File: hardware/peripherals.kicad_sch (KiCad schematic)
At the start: 0 parts

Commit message: First draft of audio amplifier
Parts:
- added C1: 0.1µF, symbol Device:C
- added C2: 10µF, symbol Device:C
- added C3, C4: 220pF, symbol Device:C
- added FB1, FB2: FerriteBead_Small, symbol Device:FerriteBead_Small
- added R1: 1M, symbol Device:R
- added U1: MAX98357A, Package_DFN_QFN:TQFN-16-1EP_3x3mm_P0.5mm_EP1.23x1.23mm, symbol Audio:MAX98357A
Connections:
- new net: C4.1, FB1.2
- new net: C1.1, C2.1, U1.7 (VDD), U1.8 (VDD)
- new net: R1.2, U1.1 (DIN)
- new net: FB2.1, U1.10 (OUTN)
- new net: FB1.1, U1.9 (OUTP)
- new net: C3.1, FB2.2
- new net GND: C1.2, C2.2, C3.2, C4.2, U1.11 (GND), U1.15 (GND), U1.3 (GND)
- no-connect marks 0 -> 1

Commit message: Updating audio amplifier
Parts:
- added J1: Conn_01x02, symbol Connector_Generic:Conn_01x02
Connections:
- net SPEAKER_VO+: now reaches C4.1, FB1.2
- net SPEAKER_VO+: now also J1.1 (Pin_1)
- net +5V: now reaches C1.1, C2.1, U1.7 (VDD), U1.8 (VDD)
- net +5V: now also R1.1
- net SPEAKER_VO-: now reaches C3.1, FB2.2
- net SPEAKER_VO-: now also J1.2 (Pin_2)

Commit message: Adding IMU
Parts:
- added U2: BNO055, Package_LGA:LGA-28_5.2x3.8mm_P0.5mm, symbol Sensor_Motion:BNO055
- renumbered C4 to C?, C2 to C?, C3 to C?, C1 to C?, FB1 to FB?, FB2 to FB?, J1 to J?, R1 to R?, U1 to U?
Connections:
- net GND: now also U?.17 (PAD)
- net at R?.2: now also U?.4 (~{SD_MODE}); no longer U?.1 (DIN)
- net LRCLK: now reaches U?.14 (LRCLK)
- net BCLK: now reaches U?.16 (BCLK)
- net GAIN: now reaches U?.2 (GAIN_SLOT)
- new net DIN: U?.1 (DIN)
- no-connect marks 1 -> 0
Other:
- moved on the sheet: R?

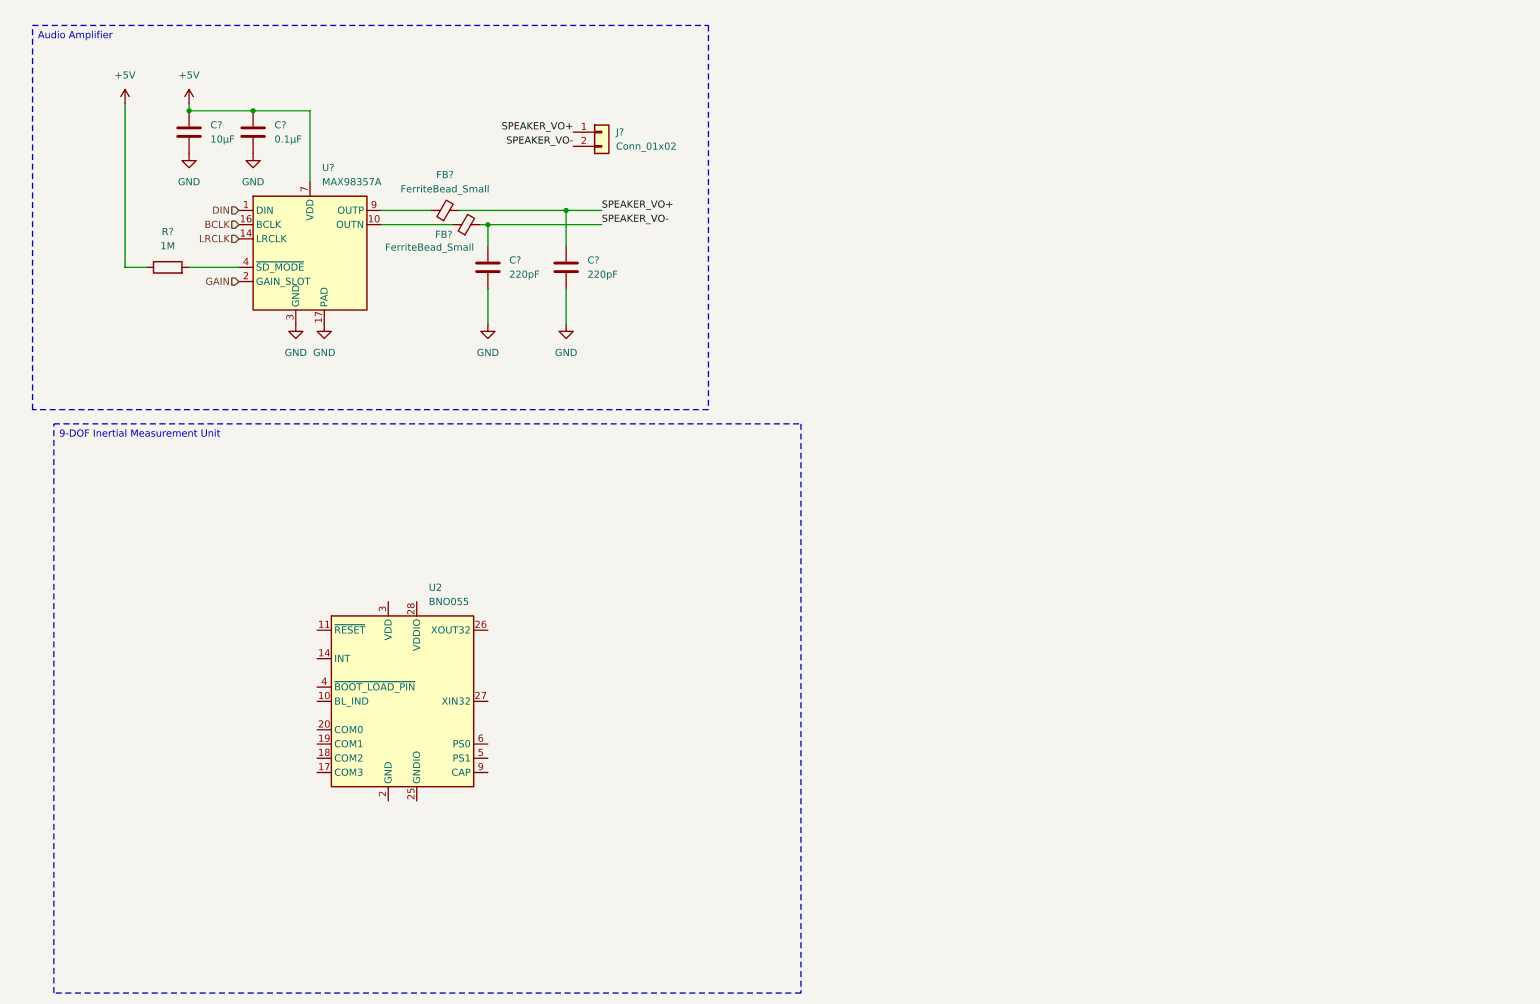
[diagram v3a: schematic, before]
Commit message: Finishing IMU schematic
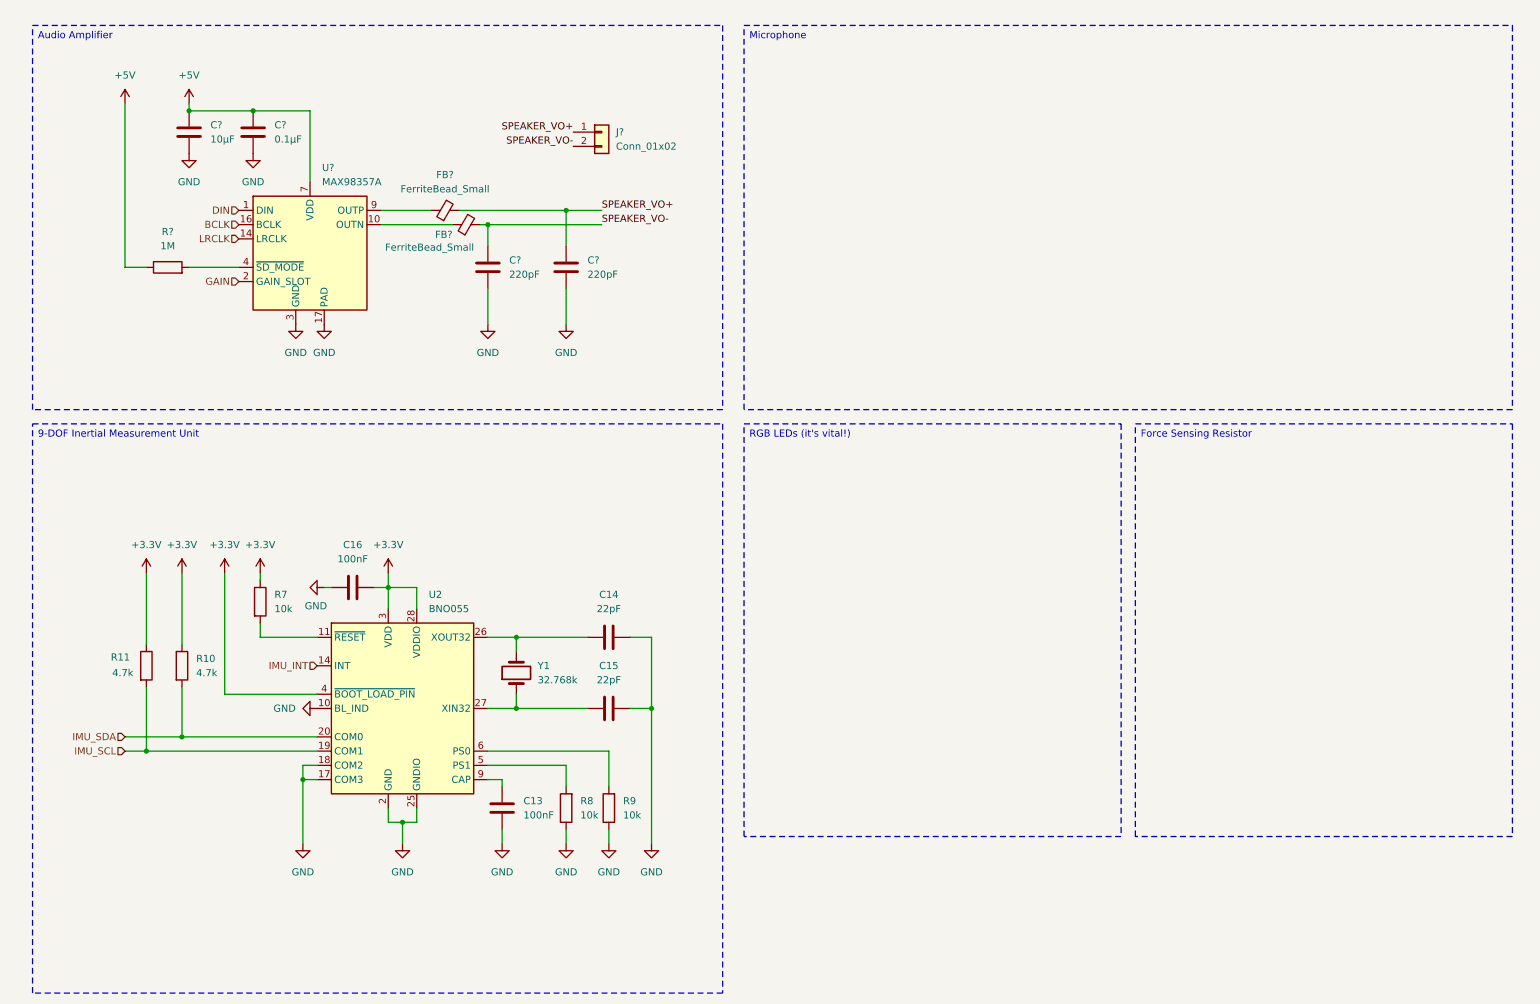
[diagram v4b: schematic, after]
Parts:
- added C13, C16: 100nF, symbol Device:C
- added C14, C15: 22pF, symbol Device:C
- added R10, R11: 4.7k, symbol Device:R
- added R7, R8, R9: 10k, symbol Device:R
- added Y1: 32.768k, symbol Device:Crystal
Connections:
- net GND: now also U2.10 (BL_IND), U2.17 (COM3), U2.18 (COM2), U2.2 (GND), U2.25 (GNDIO), C13.2, C14.2, C15.2, C16.1, R8.1, R9.1
- net at U2.11 (~{RESET}): now also R7.2
- net IMU_INT: now reaches U2.14 (INT)
- net IMU_SCL: now reaches U2.19 (COM1)
- net IMU_SCL: now also R11.2
- net IMU_SDA: now reaches U2.20 (COM0)
- net IMU_SDA: now also R10.2
- net at U2.26 (XOUT32): now also C14.1, Y1.2
- net at U2.27 (XIN32): now also C15.1, Y1.1
- net +3.3V: now reaches U2.28 (VDDIO)
- net +3.3V: now also U2.3 (VDD), U2.4 (~{BOOT_LOAD_PIN}), C16.2, R10.1, R11.1, R7.1
- net at U2.5 (PS1): now also R8.2
- net at U2.6 (PS0): now also R9.2
- net at U2.9 (CAP): now also C13.1
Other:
- moved on the sheet: U2

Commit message: Adding Force Resistive Sensor
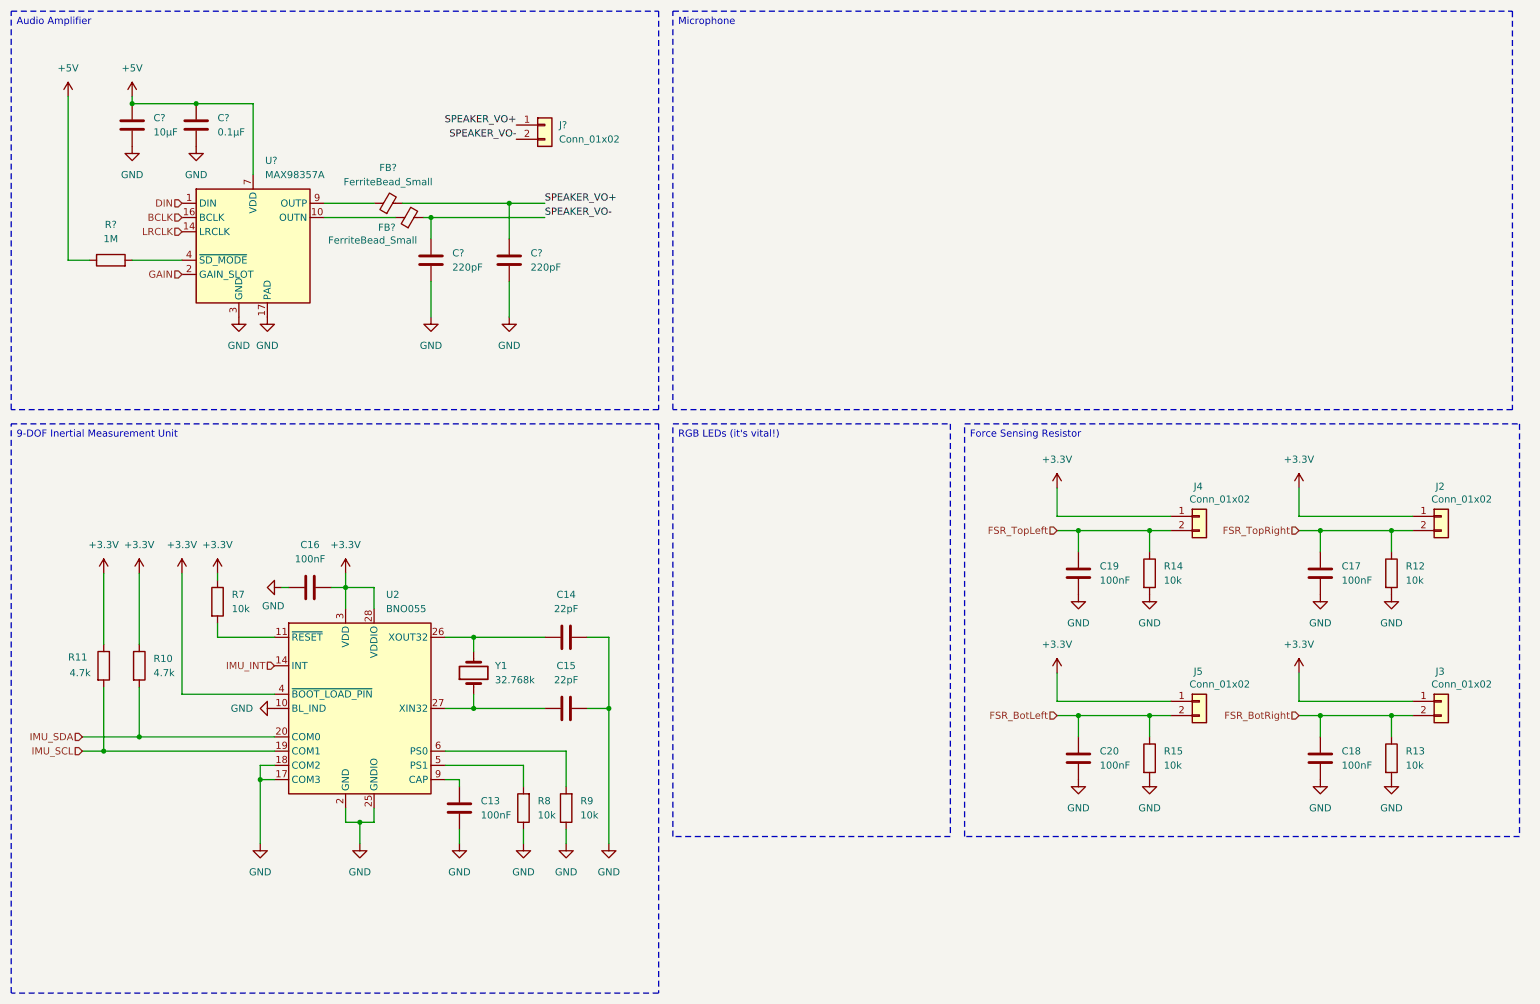
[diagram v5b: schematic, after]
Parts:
- added C17, C18, C19, C20: 100nF, symbol Device:C
- added J2, J3, J4, J5: Conn_01x02, symbol Connector_Generic:Conn_01x02
- added R12, R13, R14, R15: 10k, symbol Device:R
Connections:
- net +3.3V: now also J2.1 (Pin_1), J3.1 (Pin_1), J4.1 (Pin_1), J5.1 (Pin_1)
- net GND: now also C17.2, C18.2, C19.2, C20.2, R12.2, R13.2, R14.2, R15.2
- new net FSR_BotLeft: C20.1, J5.2 (Pin_2), R15.1
- new net FSR_BotRight: C18.1, J3.2 (Pin_2), R13.1
- new net FSR_TopLeft: C19.1, J4.2 (Pin_2), R14.1
- new net FSR_TopRight: C17.1, J2.2 (Pin_2), R12.1
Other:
- moved on the sheet: C13, C14, C15, C16, C?, FB?, J?, R10, R11, R7, R8, R9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

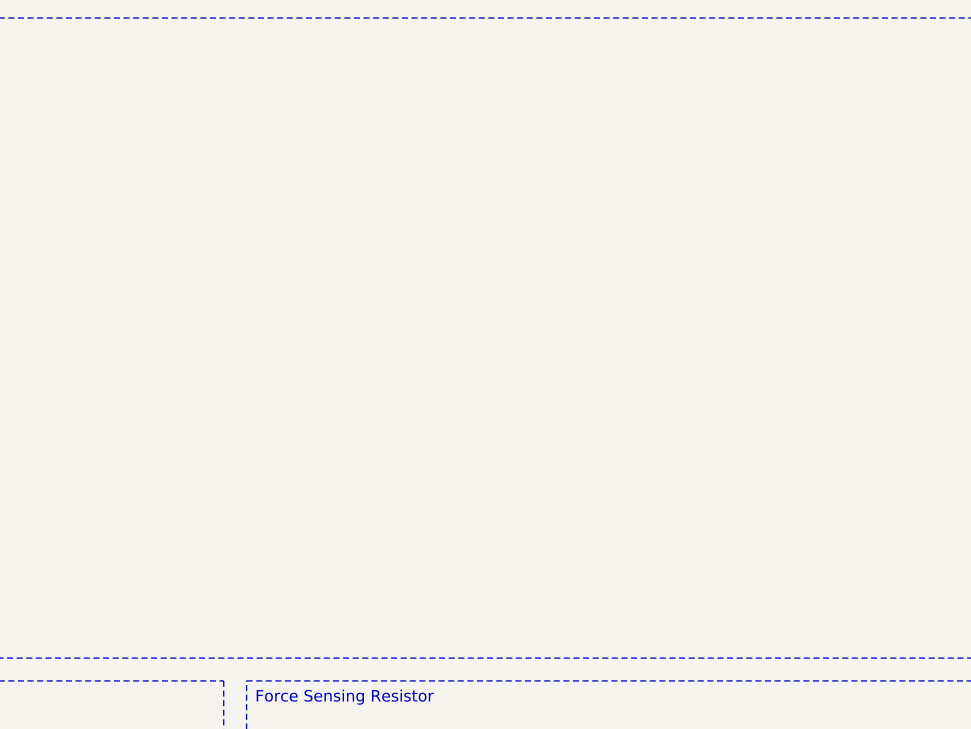
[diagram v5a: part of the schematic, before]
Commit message: Updating microphone schematic
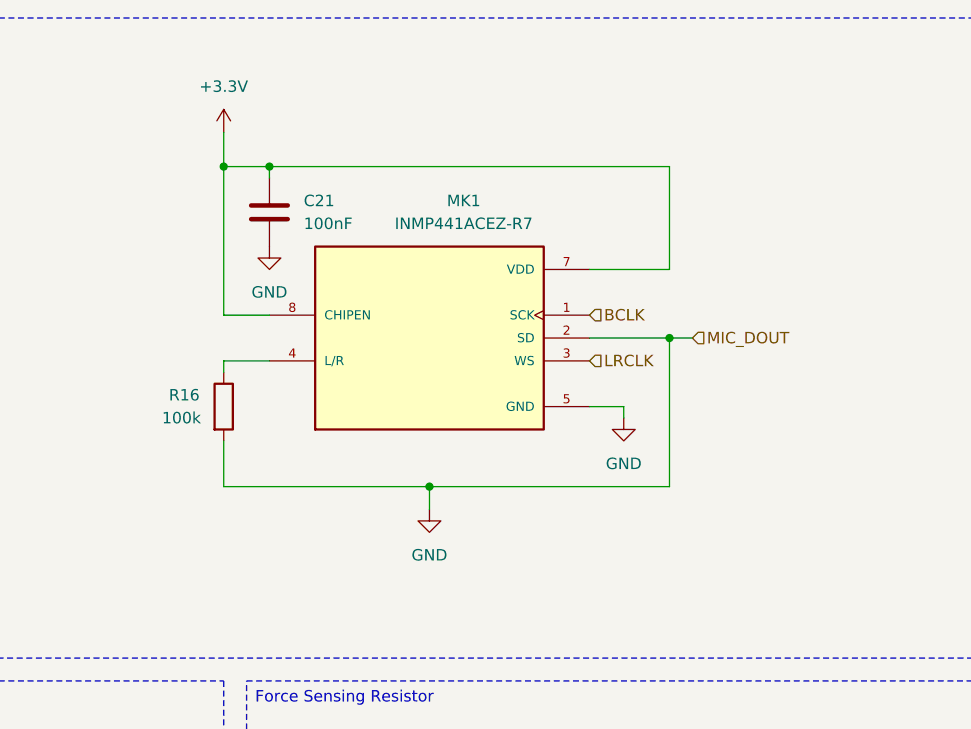
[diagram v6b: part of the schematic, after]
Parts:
- added C21: 100nF, symbol Device:C
- added MK1: INMP441ACEZ-R7, INMP441ACEZ-R7:MIC_INMP441ACEZ-R7, symbol INMP441ACEZ-R7:INMP441ACEZ-R7
- added R16: 100k, symbol Device:R
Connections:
- net +3.3V: now also C21.1, MK1.7 (VDD), MK1.8 (CHIPEN)
- net BCLK: now also MK1.1 (SCK)
- net GND: now also C21.2, MK1.2 (SD), MK1.5 (GND), MK1.6 (GND), MK1.9 (GND), R16.2
- net LRCLK: now also MK1.3 (WS)
- new net: MK1.4 (L/R), R16.1

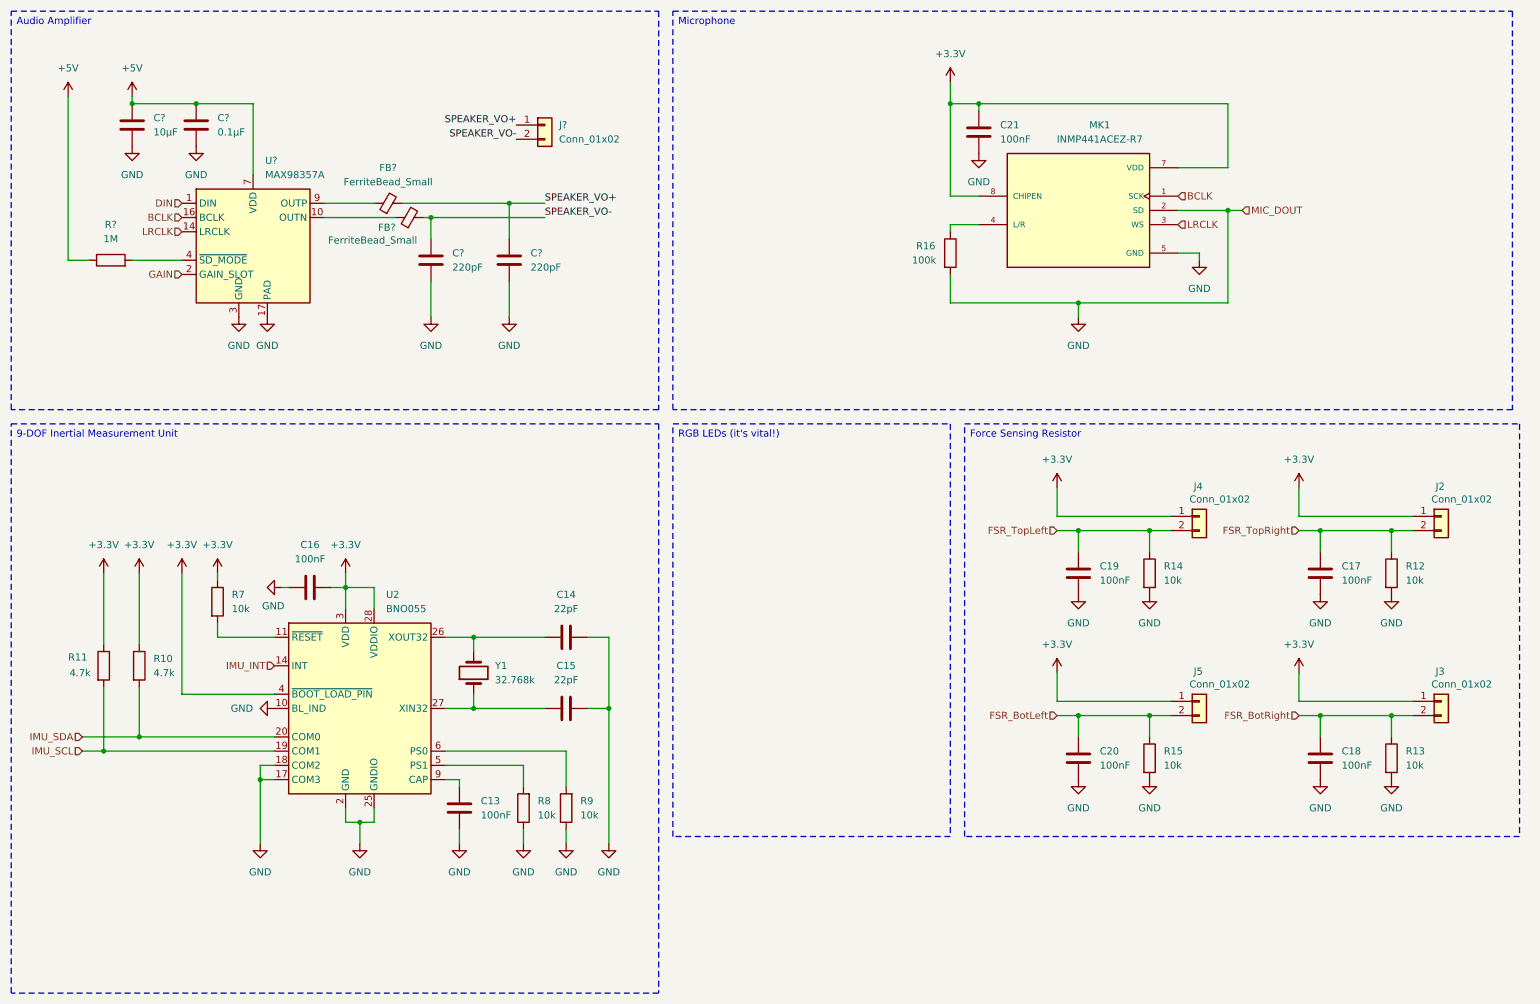
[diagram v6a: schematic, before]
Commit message: Updating peripherals
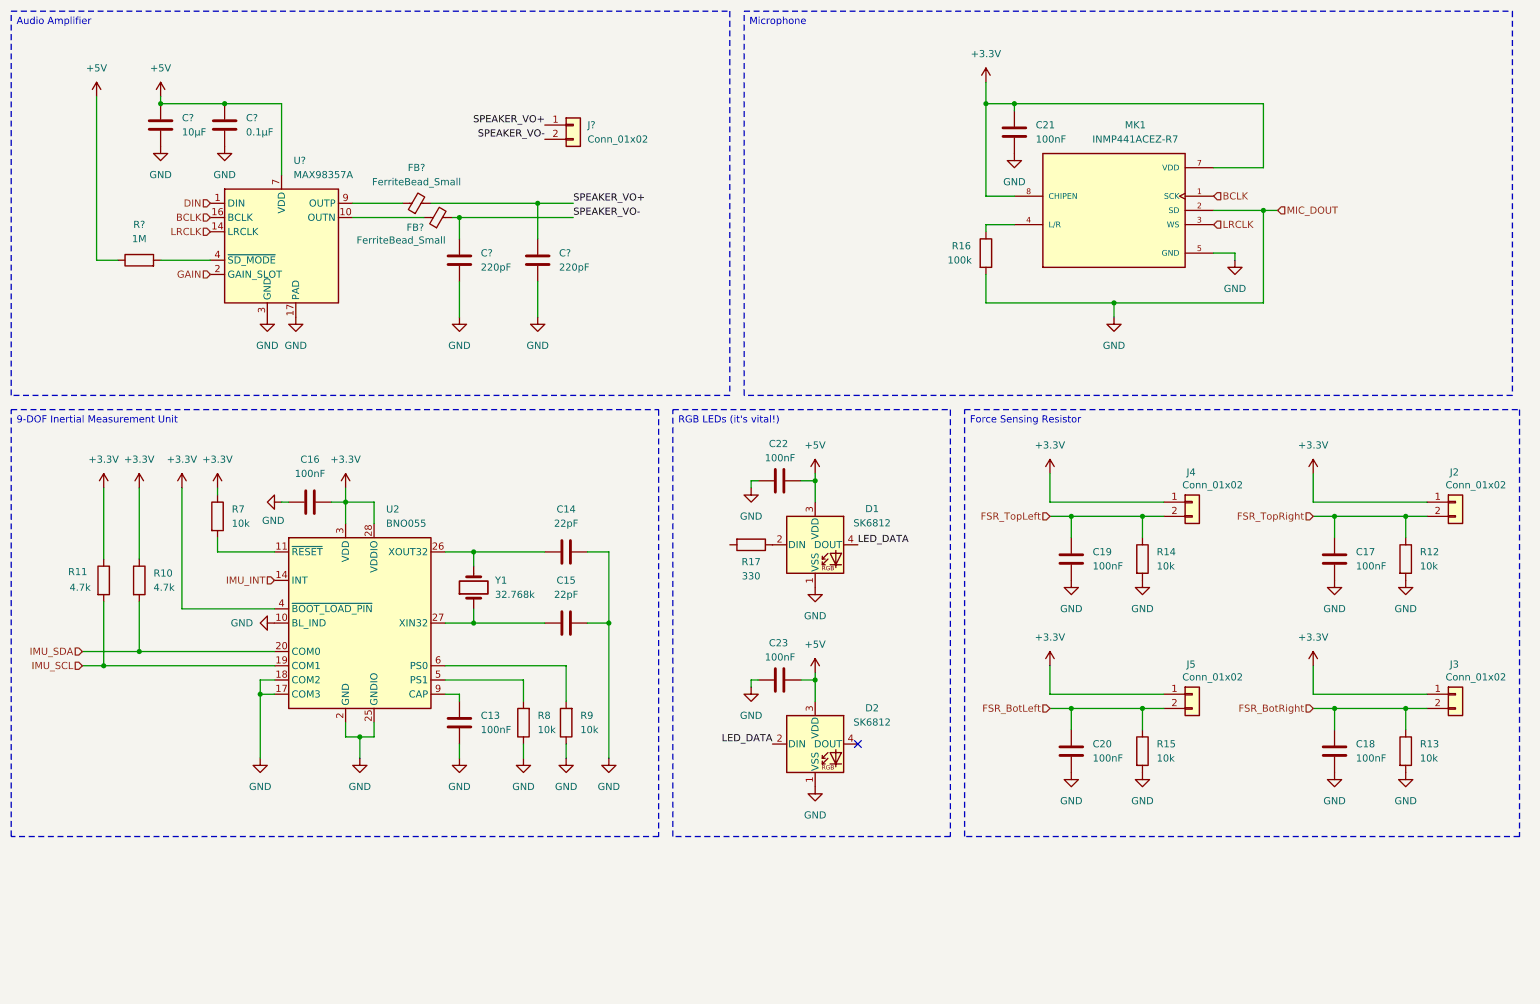
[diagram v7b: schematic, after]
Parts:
- added C22, C23: 100nF, symbol Device:C
- added D1, D2: SK6812, LED_SMD:LED_SK6812_PLCC4_5.0x5.0mm_P3.2mm, symbol LED:SK6812
- added R17: 330, symbol Device:R
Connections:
- net +5V: now also C22.2, C23.2, D1.3 (VDD), D2.3 (VDD)
- net GND: now also C22.1, C23.1, D1.1 (VSS), D2.1 (VSS)
- new net: D1.2 (DIN), R17.1
- new net LED_DATA: D1.4 (DOUT), D2.2 (DIN)
- no-connect marks 0 -> 1
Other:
- company: (none) -> Chroma
- title: (none) -> Chromapi's Peripherals
- moved on the sheet: C13, C14, C15, C16, C17, C18, C19, C20, C21, C?, FB?, J2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
